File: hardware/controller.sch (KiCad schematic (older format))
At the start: 0 parts

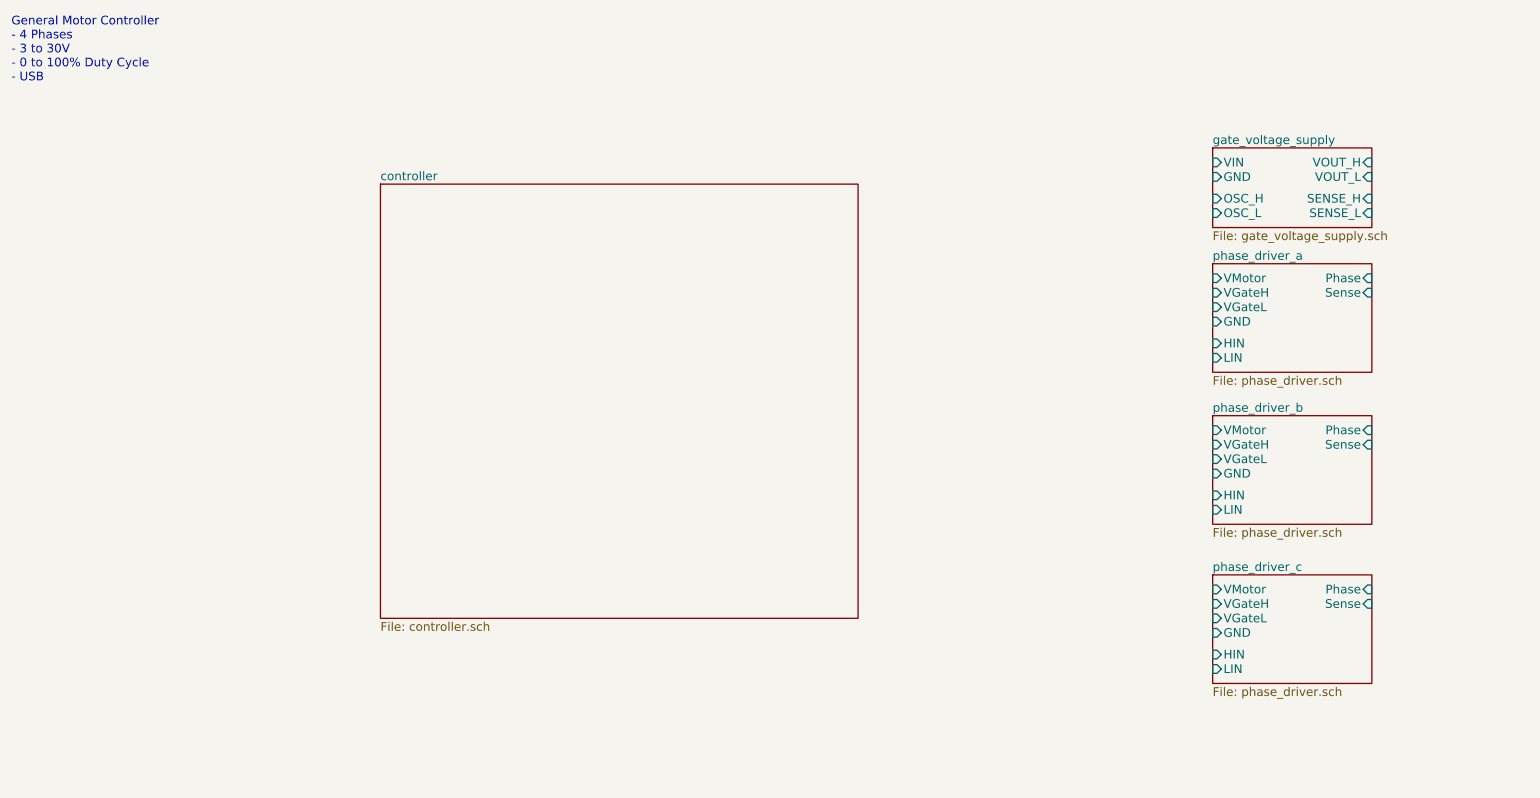
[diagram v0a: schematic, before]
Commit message: vgate, fet driver
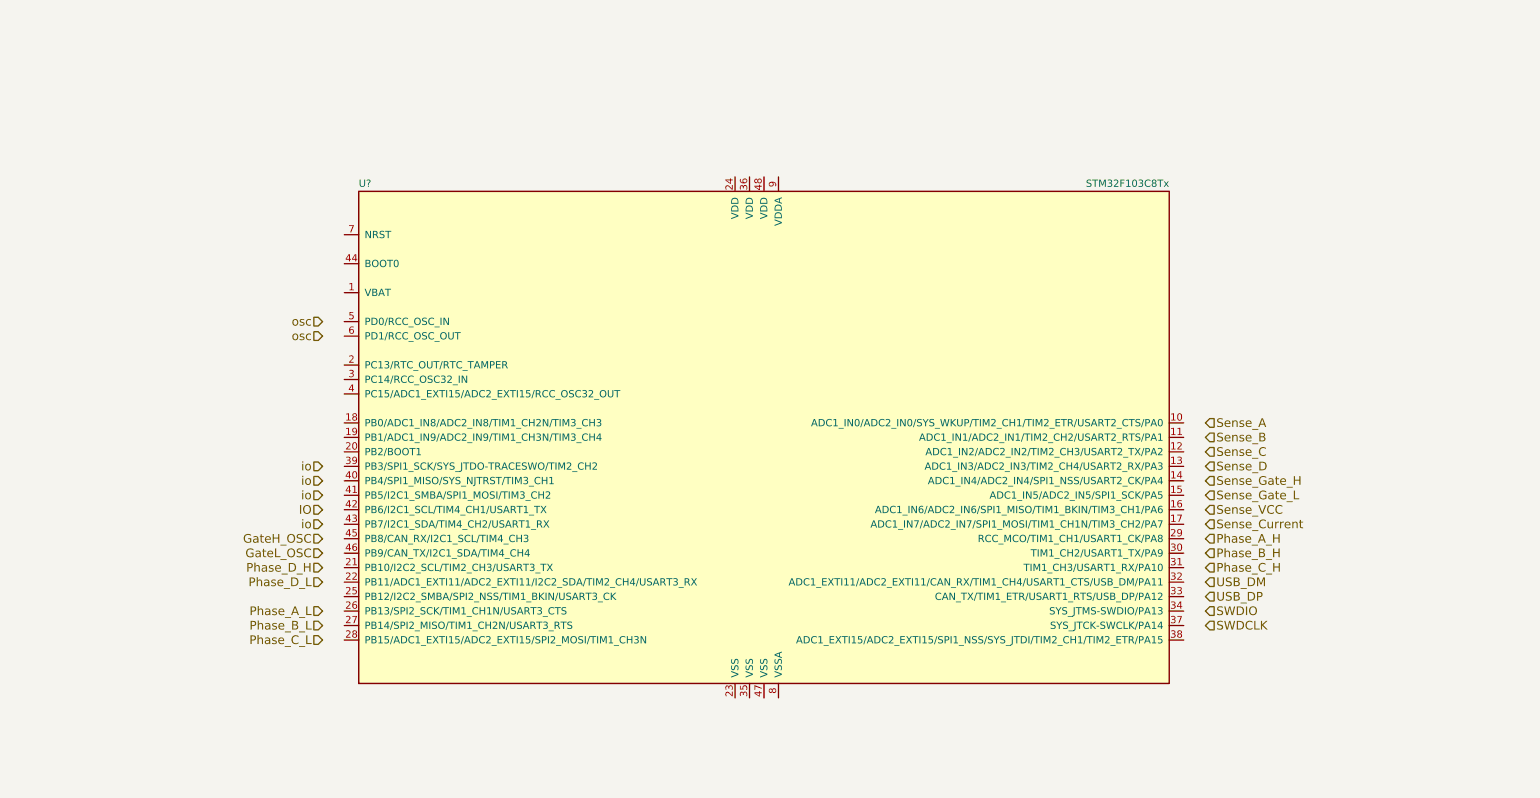
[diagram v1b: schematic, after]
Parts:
- added U?: STM32F103C8Tx, Housings_QFP:LQFP-48_7x7mm_Pitch0.5mm, symbol STM32F103C8Tx
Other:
- note removed: "General Motor Controller\n- 4 Phases\n- 3 to 30V\n- 0 to 100% Duty Cycle\n- USB"
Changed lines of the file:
@@
 $Descr A4 11693 8268
 encoding utf-8
-Sheet 1 6
+Sheet 6 6
 Title ""
 Date ""
@@
 Comment4 ""
 $EndDescr
-$Sheet
-S 8850 2250 1100 750
-U 5AE5B5EB
-F0 "phase_driver_a" 60
-F1 "phase_driver.sch" 60
-F2 "HIN" I L 8850 2800 60
-F3 "LIN" I L 8850 2900 60
-F4 "Phase" I R 9950 2350 60
-F5 "VGateH" I L 8850 2450 60
-F6 "VMotor" I L 8850 2350 60
-F7 "GND" I L 8850 2650 60
-F8 "VGateL" I L 8850 2550 60
-F9 "Sense" I R 9950 2450 60
-$EndSheet
-$Sheet
-S 8850 3300 1100 750
-U 5AE70BCE
-F0 "phase_driver_b" 60
-F1 "phase_driver.sch" 60
-F2 "HIN" I L 8850 3850 60
-F3 "LIN" I L 8850 3950 60
-F4 "Phase" I R 9950 3400 60
-F5 "VGateH" I L 8850 3500 60
-F6 "VMotor" I L 8850 3400 60
-F7 "GND" I L 8850 3700 60
-F8 "VGateL" I L 8850 3600 60
-F9 "Sense" I R 9950 3500 60
-$EndSheet
-$Sheet
-S 8850 4400 1100 750
-U 5AE71113
-F0 "phase_driver_c" 60
-F1 "phase_driver.sch" 60
-F2 "HIN" I L 8850 4950 60
-F3 "LIN" I L 8850 5050 60
-F4 "Phase" I R 9950 4500 60
-F5 "VGateH" I L 8850 4600 60
-F6 "VMotor" I L 8850 4500 60
-F7 "GND" I L 8850 4800 60
-F8 "VGateL" I L 8850 4700 60
-F9 "Sense" I R 9950 4600 60
-$EndSheet
-$Sheet
-S 8850 1450 1100 550
-U 5AE7184D
-F0 "gate_voltage_supply" 60
-F1 "gate_voltage_supply.sch" 60
-F2 "OSC_L" I L 8850 1900 60
-F3 "VIN" I L 8850 1550 60
-F4 "GND" I L 8850 1650 60
-F5 "VOUT_L" I R 9950 1650 60
-F6 "OSC_H" I L 8850 1800 60
-F7 "VOUT_H" I R 9950 1550 60
-F8 "SENSE_H" I R 9950 1800 60
-F9 "SENSE_L" I R 9950 1900 60
-$EndSheet
-Text Notes 550  1000 0    60   ~ 0
-General Motor Controller\n- 4 Phases\n- 3 to 30V\n- 0 to 100% Duty Cycle\n- USB
-$Sheet
-S 3100 1700 3300 3000
-U 5AE8CF0A
-F0 "controller" 60
-F1 "controller.sch" 60
-$EndSheet
+$Comp
+L STM32F103C8Tx U?
+U 1 1 5AE8D453
+P 5750 3450
+F 0 "U?" H 2950 5175 50  0000 L BNN
+F 1 "STM32F103C8Tx" H 8550 5175 50  0000 R BNN
+F 2 "Housings_QFP:LQFP-48_7x7mm_Pitch0.5mm" H 8550 5125 50  0001 R TNN
+F 3 "" H 5750 3450 50  0001 C CNN
+	1    5750 3450
+	1    0    0    -1
+$EndComp
+Text HLabel 8800 4150 2    60   Input ~ 0
+Phase_A_H
+Text HLabel 8800 4250 2    60   Input ~ 0
+Phase_B_H
+Text HLabel 8800 4350 2    60   Input ~ 0
+Phase_C_H
+Text HLabel 2700 4650 0    60   Input ~ 0
+Phase_A_L
+Text HLabel 2700 4750 0    60   Input ~ 0
+Phase_B_L
+Text HLabel 2700 4850 0    60   Input ~ 0
+Phase_C_L
+Text HLabel 8800 4450 2    60   Input ~ 0
+USB_DM
+Text HLabel 8800 4550 2    60   Input ~ 0
+USB_DP
+Text HLabel 8800 4650 2    60   Input ~ 0
+SWDIO
+Text HLabel 8800 4750 2    60   Input ~ 0
+SWDCLK
+Text HLabel 2700 3950 0    60   Input ~ 0
+IO
+Text HLabel 2700 4050 0    60   Input ~ 0
+io
+Text HLabel 2700 3650 0    60   Input ~ 0
+io
+Text HLabel 2700 3750 0    60   Input ~ 0
+io
+Text HLabel 2700 3850 0    60   Input ~ 0
+io
+Text HLabel 2700 2650 0    60   Input ~ 0
+osc
+Text HLabel 2700 2750 0    60   Input ~ 0
+osc
+Text HLabel 8800 3350 2    60   Input ~ 0
+Sense_A
+Text HLabel 8800 3450 2    60   Input ~ 0
+Sense_B
+Text HLabel 8800 3550 2    60   Input ~ 0
+Sense_C
+Text HLabel 8800 3650 2    60   Input ~ 0
+Sense_D
+Text HLabel 8800 3750 2    60   Input ~ 0
+Sense_Gate_H
+Text HLabel 8800 3850 2    60   Input ~ 0
+Sense_Gate_L
+Text HLabel 8800 3950 2    60   Input ~ 0
+Sense_VCC
+Text HLabel 8800 4050 2    60   Input ~ 0
+Sense_Current
+Text HLabel 2700 4350 0    60   Input ~ 0
+Phase_D_H
+Text HLabel 2700 4450 0    60   Input ~ 0
+Phase_D_L
+Text HLabel 2700 4150 0    60   Input ~ 0
+GateH_OSC
+Text HLabel 2700 4250 0    60   Input ~ 0
+GateL_OSC
 $EndSCHEMATC

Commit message: power, mcu
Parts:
- added C1, C2: 10p, Capacitors_SMD:C_0603, symbol C
- added C3, C4: 47p, Capacitors_SMD:C_0603, symbol C
- added R10: 1.5k, Resistors_SMD:R_0603, symbol R
- added R8, R9: 22R, Resistors_SMD:R_0603, symbol R
- added Y1: Crystal_GND24, Crystals:Crystal_SMD_3225-4pin_3.2x2.5mm, symbol Crystal_GND24
- gave numbers to parts that had none: 1
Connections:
- net SWDCLK: now also U1.37 (SYS_JTCK-SWCLK/PA14)
- net SWDIO: now also U1.34 (SYS_JTMS-SWDIO/PA13)
- net USB_DM: now also C3.2, R8.2
- net USB_DP: now also C4.1, R10.1, R9.2
- net VDD: now reaches U1.1 (VBAT)
- net VDD: now also U1.24 (VDD), U1.36 (VDD), U1.48 (VDD), U1.9 (VDDA), R10.2
- net SENSE_1: now reaches U1.10 (ADC1_IN0/ADC2_IN0/SYS_WKUP/TIM2_CH1/TIM2_ETR/USART2_CTS/PA0)
- net SENSE_2: now reaches U1.11 (ADC1_IN1/ADC2_IN1/TIM2_CH2/USART2_RTS/PA1)
- net SENSE_3: now reaches U1.12 (ADC1_IN2/ADC2_IN2/TIM2_CH3/USART2_TX/PA2)
- net SENSE_4: now reaches U1.13 (ADC1_IN3/ADC2_IN3/TIM2_CH4/USART2_RX/PA3)
- net SENSE_Vgh: now reaches U1.14 (ADC1_IN4/ADC2_IN4/SPI1_NSS/USART2_CK/PA4)
- net SENSE_Vgl: now reaches U1.15 (ADC1_IN5/ADC2_IN5/SPI1_SCK/PA5)
- net SENSE_Vmotor: now reaches U1.16 (ADC1_IN6/ADC2_IN6/SPI1_MISO/TIM1_BKIN/TIM3_CH1/PA6)
- net PA7: now reaches U1.17 (ADC1_IN7/ADC2_IN7/SPI1_MOSI/TIM1_CH1N/TIM3_CH2/PA7)
- net PB0: now reaches U1.18 (PB0/ADC1_IN8/ADC2_IN8/TIM1_CH2N/TIM3_CH3)
- net PB1: now reaches U1.19 (PB1/ADC1_IN9/ADC2_IN9/TIM1_CH3N/TIM3_CH4)
- net PC13: now reaches U1.2 (PC13/RTC_OUT/RTC_TAMPER)
- net PB2: now reaches U1.20 (PB2/BOOT1)
- net PHASE_4_H: now reaches U1.21 (PB10/I2C2_SCL/TIM2_CH3/USART3_TX)
- net PHASE_4_L: now reaches U1.22 (PB11/ADC1_EXTI11/ADC2_EXTI11/I2C2_SDA/TIM2_CH4/USART3_RX)
- net GND: now reaches U1.23 (VSS)
- net GND: now also U1.35 (VSS), U1.47 (VSS), U1.8 (VSSA), C1.2, C2.2, C3.1, C4.2
- net PB12: now reaches U1.25 (PB12/I2C2_SMBA/SPI2_NSS/TIM1_BKIN/USART3_CK)
- net PHASE_1_L: now reaches U1.26 (PB13/SPI2_SCK/TIM1_CH1N/USART3_CTS)
- net PHASE_2_L: now reaches U1.27 (PB14/SPI2_MISO/TIM1_CH2N/USART3_RTS)
- net PHASE_3_L: now reaches U1.28 (PB15/ADC1_EXTI15/ADC2_EXTI15/SPI2_MOSI/TIM1_CH3N)
- net PHASE_1_H: now reaches U1.29 (RCC_MCO/TIM1_CH1/USART1_CK/PA8)
- net PC14: now reaches U1.3 (PC14/RCC_OSC32_IN)
- net PHASE_2_H: now reaches U1.30 (TIM1_CH2/USART1_TX/PA9)
- net PHASE_3_H: now reaches U1.31 (TIM1_CH3/USART1_RX/PA10)
- net at U1.32 (ADC1_EXTI11/ADC2_EXTI11/CAN_RX/TIM1_CH4/USART1_CTS/USB_DM/PA11): now also R8.1
- net at U1.33 (CAN_TX/TIM1_ETR/USART1_RTS/USB_DP/PA12): now also R9.1
- net PA15: now reaches U1.38 (ADC1_EXTI15/ADC2_EXTI15/SPI1_NSS/SYS_JTDI/TIM2_CH1/TIM2_ETR/PA15)
- net PB3: now reaches U1.39 (PB3/SPI1_SCK/SYS_JTDO-TRACESWO/TIM2_CH2)
- net PC15: now reaches U1.4 (PC15/ADC1_EXTI15/ADC2_EXTI15/RCC_OSC32_OUT)
- net PB4: now reaches U1.40 (PB4/SPI1_MISO/SYS_NJTRST/TIM3_CH1)
- net PB5: now reaches U1.41 (PB5/I2C1_SMBA/SPI1_MOSI/TIM3_CH2)
- net PB6: now reaches U1.42 (PB6/I2C1_SCL/TIM4_CH1/USART1_TX)
- net PB7: now reaches U1.43 (PB7/I2C1_SDA/TIM4_CH2/USART1_RX)
- net BOOT0: now reaches U1.44 (BOOT0)
- net CLK_Vgh: now reaches U1.45 (PB8/CAN_RX/I2C1_SCL/TIM4_CH3)
- net CLK_Vgl: now reaches U1.46 (PB9/CAN_TX/I2C1_SDA/TIM4_CH4)
- net at U1.5 (PD0/RCC_OSC_IN): now also Y1.1
- net at U1.6 (PD1/RCC_OSC_OUT): now also Y1.3
- net RESET: now reaches U1.7 (NRST)
- new net: C1.1, Y1.2
- new net: C2.1, Y1.4
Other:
- moved on the sheet: U1

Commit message: phase routet
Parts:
- added C5, C6, C7, C8: 100n, Capacitors_SMD:C_0603, symbol C
- Y1: value Crystal_GND24 -> 16Mhz
- renumbered C4 to C10, C1 to C3, C2 to C4, C3 to C9
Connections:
- net GND: now also C5.2, C6.2, C7.2, C8.2
- net VDD: now also C5.1, C6.1, C7.1, C8.1
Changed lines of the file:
@@
 P 2100 3100
 F 0 "Y1" V 2300 3250 50  0000 L CNN
-F 1 "Crystal_GND24" V 2225 3225 50  0000 L CNN
+F 1 "16Mhz" V 2225 3225 50  0000 L CNN
 F 2 "Crystals:Crystal_SMD_3225-4pin_3.2x2.5mm" H 2100 3100 50  0001 C CNN
 F 3 "" H 2100 3100 50  0001 C CNN
@@
 	2350 2800 1750 2800
 $Comp
-L C C1
+L C C3
 U 1 1 5AE86EDC
 P 1600 2800
-F 0 "C1" H 1625 2900 50  0000 L CNN
+F 0 "C3" H 1625 2900 50  0000 L CNN
 F 1 "10p" H 1625 2700 50  0000 L CNN
 F 2 "Capacitors_SMD:C_0603" H 1638 2650 50  0001 C CNN
@@
 $EndComp
 $Comp
-L C C2
+L C C4
 U 1 1 5AE86F0D
 P 1600 3100
-F 0 "C2" H 1625 3200 50  0000 L CNN
+F 0 "C4" H 1625 3200 50  0000 L CNN
 F 1 "10p" H 1625 3000 50  0000 L CNN
 F 2 "Capacitors_SMD:C_0603" H 1638 2950 50  0001 C CNN
@@
 	10150 4800 10550 4800
 $Comp
-L C C4
+L C C10
 U 1 1 5AED5E8C
 P 10450 5200
-F 0 "C4" H 10475 5300 50  0000 L CNN
+F 0 "C10" H 10475 5300 50  0000 L CNN
 F 1 "47p" H 10475 5100 50  0000 L CNN
 F 2 "Capacitors_SMD:C_0603" H 10488 5050 50  0001 C CNN
@@
 	10450 5400 10550 5400
 $Comp
-L C C3
+L C C9
 U 1 1 5AED626C
 P 10450 4600
-F 0 "C3" H 10475 4700 50  0000 L CNN
+F 0 "C9" H 10475 4700 50  0000 L CNN
 F 1 "47p" H 10475 4500 50  0000 L CNN
 F 2 "Capacitors_SMD:C_0603" H 10488 4450 50  0001 C CNN
@@
 Wire Wire Line
 	6000 5650 6000 5800
+Text HLabel 6150 850  0    60   Input ~ 0
+VDD
+$Comp
+L C C5
+U 1 1 5AE9A47C
+P 6300 1150
+F 0 "C5" H 6325 1250 50  0000 L CNN
+F 1 "100n" H 6325 1050 50  0000 L CNN
+F 2 "Capacitors_SMD:C_0603" H 6338 1000 50  0001 C CNN
+F 3 "" H 6300 1150 50  0001 C CNN
+	1    6300 1150
+	1    0    0    -1
+$EndComp
+$Comp
+L C C6
+U 1 1 5AE9A4AB
+P 6600 1150
+F 0 "C6" H 6625 1250 50  0000 L CNN
+F 1 "100n" H 6625 1050 50  0000 L CNN
+F 2 "Capacitors_SMD:C_0603" H 6638 1000 50  0001 C CNN
+F 3 "" H 6600 1150 50  0001 C CNN
+	1    6600 1150
+	1    0    0    -1
+$EndComp
+$Comp
+L C C7
+U 1 1 5AE9A4FD
+P 6900 1150
+F 0 "C7" H 6925 1250 50  0000 L CNN
+F 1 "100n" H 6925 1050 50  0000 L CNN
+F 2 "Capacitors_SMD:C_0603" H 6938 1000 50  0001 C CNN
+F 3 "" H 6900 1150 50  0001 C CNN
+	1    6900 1150
+	1    0    0    -1
+$EndComp
+Wire Wire Line
+	6150 850  7200 850
+Wire Wire Line
+	6300 850  6300 1000
+Wire Wire Line
+	6600 850  6600 1000
+Connection ~ 6300 850
+Wire Wire Line
+	6900 850  6900 1000
+Connection ~ 6600 850
+Wire Wire Line
+	7200 850  7200 1000
+Connection ~ 6900 850
+Text HLabel 6150 1450 0    60   Input ~ 0
+GND
+Wire Wire Line
+	6150 1450 7200 1450
+Wire Wire Line
+	6300 1450 6300 1300
+Wire Wire Line
+	6600 1450 6600 1300
+Connection ~ 6300 1450
+Wire Wire Line
+	6900 1450 6900 1300
+Connection ~ 6600 1450
+Wire Wire Line
+	7200 1450 7200 1300
+Connection ~ 6900 1450
+$Comp
+L C C8
+U 1 1 5AE9A52E
+P 7200 1150
+F 0 "C8" H 7225 1250 50  0000 L CNN
+F 1 "100n" H 7225 1050 50  0000 L CNN
+F 2 "Capacitors_SMD:C_0603" H 7238 1000 50  0001 C CNN
+F 3 "" H 7200 1150 50  0001 C CNN
+	1    7200 1150
+	1    0    0    -1
+$EndComp
 $EndSCHEMATC

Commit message: change to kicad 5
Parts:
- C10, C3, C4, C5, C6, C7, C8, C9: footprint Capacitors_SMD:C_0603 -> Capacitor_SMD:C_0603_1608Metric; symbol C -> Device:C
- R10, R8, R9: footprint Resistors_SMD:R_0603 -> Resistor_SMD:R_0603_1608Metric; symbol R -> Device:R
- U1: footprint Housings_QFP:LQFP-48_7x7mm_Pitch0.5mm -> Package_QFP:LQFP-48_7x7mm_P0.5mm; symbol STM32F103C8Tx -> MCU_ST_STM32F1:STM32F103C8Tx
- Y1: footprint Crystals:Crystal_SMD_3225-4pin_3.2x2.5mm -> Crystal:Crystal_SMD_3225-4Pin_3.2x2.5mm; symbol Crystal_GND24 -> Device:Crystal_GND24
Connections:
- wire segments 89 -> 106
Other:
- moved on the sheet: C10, C3, C4, C9, R10, R8, R9, Y1

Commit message: smaller footprints
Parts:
- C10, C3, C4, C5, C6, C7, C8, C9: footprint Capacitor_SMD:C_0603_1608Metric -> _Generic:0603_Small
- R10, R8, R9: footprint Resistor_SMD:R_0603_1608Metric -> _Generic:0603_Small
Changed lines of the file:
@@
 F 0 "C3" H 3825 2800 50  0000 L CNN
 F 1 "10p" H 3825 2600 50  0000 L CNN
-F 2 "Capacitor_SMD:C_0603_1608Metric" H 3838 2550 50  0001 C CNN
+F 2 "_Generic:0603_Small" H 3838 2550 50  0001 C CNN
 F 3 "" H 3800 2700 50  0001 C CNN
 	1    3800 2700
@@
 F 0 "C4" H 3825 3100 50  0000 L CNN
 F 1 "10p" H 3825 2900 50  0000 L CNN
-F 2 "Capacitor_SMD:C_0603_1608Metric" H 3838 2850 50  0001 C CNN
+F 2 "_Generic:0603_Small" H 3838 2850 50  0001 C CNN
 F 3 "" H 3800 3000 50  0001 C CNN
 	1    3800 3000
@@
 F 0 "R9" V 7780 4900 50  0000 C CNN
 F 1 "22R" V 7700 4900 50  0000 C CNN
-F 2 "Resistor_SMD:R_0603_1608Metric" V 7630 4900 50  0001 C CNN
+F 2 "_Generic:0603_Small" V 7630 4900 50  0001 C CNN
 F 3 "" H 7700 4900 50  0001 C CNN
 	1    7700 4900
@@
 F 0 "R8" V 7780 4700 50  0000 C CNN
 F 1 "22R" V 7700 4700 50  0000 C CNN
-F 2 "Resistor_SMD:R_0603_1608Metric" V 7630 4700 50  0001 C CNN
+F 2 "_Generic:0603_Small" V 7630 4700 50  0001 C CNN
 F 3 "" H 7700 4700 50  0001 C CNN
 	1    7700 4700
@@
 F 0 "C10" H 8175 5200 50  0000 L CNN
 F 1 "47p" H 8175 5000 50  0000 L CNN
-F 2 "Capacitor_SMD:C_0603_1608Metric" H 8188 4950 50  0001 C CNN
+F 2 "_Generic:0603_Small" H 8188 4950 50  0001 C CNN
 F 3 "" H 8150 5100 50  0001 C CNN
 	1    8150 5100
@@
 F 0 "R10" V 7980 5100 50  0000 C CNN
 F 1 "1.5k" V 7900 5100 50  0000 C CNN
-F 2 "Resistor_SMD:R_0603_1608Metric" V 7830 5100 50  0001 C CNN
+F 2 "_Generic:0603_Small" V 7830 5100 50  0001 C CNN
 F 3 "" H 7900 5100 50  0001 C CNN
 	1    7900 5100
@@
 F 0 "C9" H 8175 4600 50  0000 L CNN
 F 1 "47p" H 8175 4400 50  0000 L CNN
-F 2 "Capacitor_SMD:C_0603_1608Metric" H 8188 4350 50  0001 C CNN
+F 2 "_Generic:0603_Small" H 8188 4350 50  0001 C CNN
 F 3 "" H 8150 4500 50  0001 C CNN
 	1    8150 4500
@@
 F 0 "C5" H 6325 1250 50  0000 L CNN
 F 1 "100n" H 6325 1050 50  0000 L CNN
-F 2 "Capacitor_SMD:C_0603_1608Metric" H 6338 1000 50  0001 C CNN
+F 2 "_Generic:0603_Small" H 6338 1000 50  0001 C CNN
 F 3 "" H 6300 1150 50  0001 C CNN
 	1    6300 1150
@@
 F 0 "C6" H 6625 1250 50  0000 L CNN
 F 1 "100n" H 6625 1050 50  0000 L CNN
-F 2 "Capacitor_SMD:C_0603_1608Metric" H 6638 1000 50  0001 C CNN
+F 2 "_Generic:0603_Small" H 6638 1000 50  0001 C CNN
 F 3 "" H 6600 1150 50  0001 C CNN
 	1    6600 1150
@@
 F 0 "C7" H 6925 1250 50  0000 L CNN
 F 1 "100n" H 6925 1050 50  0000 L CNN
-F 2 "Capacitor_SMD:C_0603_1608Metric" H 6938 1000 50  0001 C CNN
+F 2 "_Generic:0603_Small" H 6938 1000 50  0001 C CNN
 F 3 "" H 6900 1150 50  0001 C CNN
 	1    6900 1150
@@
 F 0 "C8" H 7225 1250 50  0000 L CNN
 F 1 "100n" H 7225 1050 50  0000 L CNN
-F 2 "Capacitor_SMD:C_0603_1608Metric" H 7238 1000 50  0001 C CNN
+F 2 "_Generic:0603_Small" H 7238 1000 50  0001 C CNN
 F 3 "" H 7200 1150 50  0001 C CNN
 	1    7200 1150

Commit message: stm layout
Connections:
- wire segments 106 -> 110
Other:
- moved on the sheet: C3, C4
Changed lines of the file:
@@
 Wire Wire Line
 	4300 3200 4300 3150
-Wire Wire Line
-	4500 3000 4550 3000
-Wire Wire Line
-	4550 3000 4550 2700
-Wire Wire Line
-	4550 2700 3950 2700
 $Comp
 L Device:C C3
 U 1 1 5AE86EDC
-P 3800 2700
-F 0 "C3" H 3825 2800 50  0000 L CNN
-F 1 "10p" H 3825 2600 50  0000 L CNN
-F 2 "_Generic:0603_Small" H 3838 2550 50  0001 C CNN
-F 3 "" H 3800 2700 50  0001 C CNN
-	1    3800 2700
+P 3800 2800
+F 0 "C3" H 3825 2900 50  0000 L CNN
+F 1 "10p" H 3825 2700 50  0000 L CNN
+F 2 "_Generic:0603_Small" H 3838 2650 50  0001 C CNN
+F 3 "" H 3800 2800 50  0001 C CNN
+	1    3800 2800
 	0    1    1    0
 $EndComp
@@
 L Device:C C4
 U 1 1 5AE86F0D
-P 3800 3000
-F 0 "C4" H 3825 3100 50  0000 L CNN
-F 1 "10p" H 3825 2900 50  0000 L CNN
-F 2 "_Generic:0603_Small" H 3838 2850 50  0001 C CNN
-F 3 "" H 3800 3000 50  0001 C CNN
-	1    3800 3000
+P 3800 3200
+F 0 "C4" H 3825 3300 50  0000 L CNN
+F 1 "10p" H 3825 3100 50  0000 L CNN
+F 2 "_Generic:0603_Small" H 3838 3050 50  0001 C CNN
+F 3 "" H 3800 3200 50  0001 C CNN
+	1    3800 3200
 	0    1    1    0
 $EndComp
-Wire Wire Line
-	3950 3000 4100 3000
-Text HLabel 3500 2850 0    60   Input ~ 0
-GND
-Wire Wire Line
-	3500 2850 3550 2850
-Wire Wire Line
-	3550 2700 3550 2850
-Wire Wire Line
-	3550 2700 3650 2700
-Wire Wire Line
-	3550 3000 3650 3000
-Connection ~ 3550 2850
+Text HLabel 3500 3000 0    60   Input ~ 0
+GND
+Wire Wire Line
+	3500 3000 3550 3000
+Wire Wire Line
+	3550 2800 3550 3000
+Wire Wire Line
+	3550 2800 3650 2800
+Wire Wire Line
+	3550 3200 3650 3200
+Connection ~ 3550 3000
 Text HLabel 5150 3250 0    60   BiDi ~ 0
 PC13
@@
 $EndComp
 Wire Wire Line
-	3550 2850 3550 3000
+	3550 3000 3550 3200
 Wire Wire Line
 	5800 5500 5900 5500
@@
 	6200 2200 6200 2350
 Connection ~ 6100 2200
+Wire Wire Line
+	4300 2800 3950 2800
+Connection ~ 4300 2800
+Wire Wire Line
+	3950 3200 4300 3200
+Connection ~ 4300 3200
+Wire Wire Line
+	4100 3000 4050 3000
+Wire Wire Line
+	4050 2700 4050 3000
+Connection ~ 4050 3000
+Wire Wire Line
+	4050 3000 3550 3000
+Wire Wire Line
+	4500 3000 4550 3000
+Wire Wire Line
+	4550 3000 4550 2700
+Wire Wire Line
+	4050 2700 4550 2700
 $EndSCHEMATC
